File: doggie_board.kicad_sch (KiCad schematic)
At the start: 0 parts

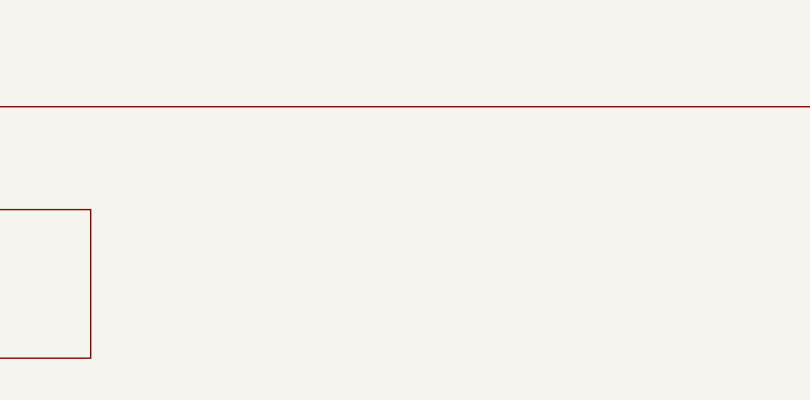
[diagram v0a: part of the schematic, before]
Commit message: Fixed ERC
Created Buck3
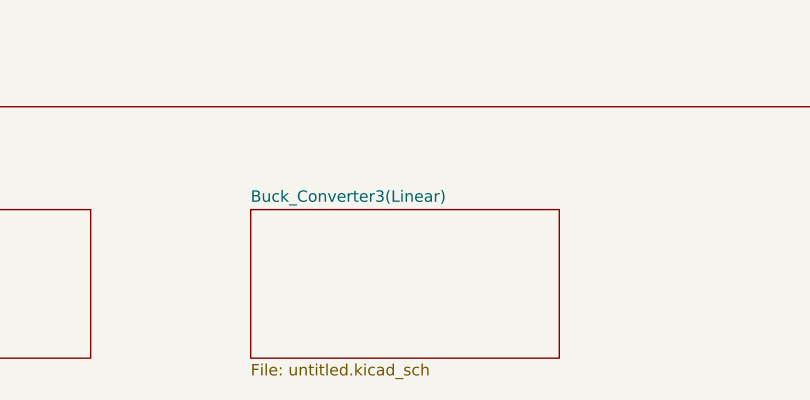
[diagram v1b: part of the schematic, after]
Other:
- added sheet Buck_Converter3(Linear) (untitled.kicad_sch)
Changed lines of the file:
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@@
 	(paper "A4")
+	(sheet
+		(at 74.93 115.57)
+		(size 34.29 16.51)
+		(exclude_from_sim no)
+		(in_bom yes)
+		(on_board yes)
+		(dnp no)
+		(fields_autoplaced yes)
+		(stroke
+			(width 0.1524)
+			(type solid)
+		)
+		(fill
+			(color 0 0 0 0.0000)
+		)
+		(property "Sheetname" "Buck_Converter3(Linear)"
+			(at 74.93 114.8584 0)
+			(effects
+				(font
+					(size 1.27 1.27)
+				)
+				(justify left bottom)
+			)
+		)
+		(property "Sheetfile" "untitled.kicad_sch"
+			(at 74.93 132.6646 0)
+			(effects
+				(font
+					(size 1.27 1.27)
+				)
+				(justify left top)
+			)
+		)
+		(instances
+			(project "doggie_board"
+				(path "/883cb7fa-3eb5-48d4-9cde-7c11307d94f0"
+					(page "5")
+				)
+			)
+		)
+	)
 	(sheet
 		(at 15.24 115.57)
